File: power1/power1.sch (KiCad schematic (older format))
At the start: 24 parts, among them P1 CONN_01X02, P2 CONN_01X04, U1 LT3633

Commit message: Few more pcb changes
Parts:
- added C13: DNI, Capacitors_Tantalum_SMD:TantalC_SizeC_EIA-6032_HandSoldering, symbol CP1
- added C14: DNI, Capacitors_SMD:C_0805_HandSoldering, symbol C
- C5: footprint Capacitors_SMD:C_0805_HandSoldering -> Capacitors_Tantalum_SMD:TantalC_SizeC_EIA-6032_HandSoldering
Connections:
- net GND: now also C13.2, C14.2
- net at L5.2, P2.4 (P4), U1.18 (Vin2)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: now also C13.1, C14.1
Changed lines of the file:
@@
 F 0 "C5" H 4450 3250 50  0000 L CNN
 F 1 "10uF 25V" H 4450 3050 50  0000 L CNN
-F 2 "Capacitors_SMD:C_0805_HandSoldering" H 4400 3150 60  0001 C CNN
+F 2 "Capacitors_Tantalum_SMD:TantalC_SizeC_EIA-6032_HandSoldering" H 4400 3150 60  0001 C CNN
 F 3 "" H 4400 3150 60  0000 C CNN
 	1    4400 3150
@@
 Text Notes 7300 4300 0    50   ~ 0
 SRP4020TA-1R0M
+$Comp
+L C C14
+U 1 1 54BD0736
+P 9300 3300
+F 0 "C14" H 9300 3400 40  0000 L CNN
+F 1 "DNI" H 9306 3215 40  0000 L CNN
+F 2 "Capacitors_SMD:C_0805_HandSoldering" H 9338 3150 30  0001 C CNN
+F 3 "" H 9300 3300 60  0000 C CNN
+	1    9300 3300
+	1    0    0    -1
+$EndComp
+$Comp
+L GND #PWR016
+U 1 1 54BD07E1
+P 9300 3500
+F 0 "#PWR016" H 9300 3500 30  0001 C CNN
+F 1 "GND" H 9300 3430 30  0001 C CNN
+F 2 "" H 9300 3500 50  0000 C CNN
+F 3 "" H 9300 3500 50  0000 C CNN
+	1    9300 3500
+	1    0    0    -1
+$EndComp
+$Comp
+L CP1 C13
+U 1 1 54BD08E0
+P 8900 3300
+F 0 "C13" H 8950 3400 50  0000 L CNN
+F 1 "DNI" H 8950 3200 50  0000 L CNN
+F 2 "Capacitors_Tantalum_SMD:TantalC_SizeC_EIA-6032_HandSoldering" H 8900 3300 60  0001 C CNN
+F 3 "" H 8900 3300 60  0000 C CNN
+	1    8900 3300
+	1    0    0    -1
+$EndComp
+$Comp
+L GND #PWR017
+U 1 1 54BD0994
+P 8900 3500
+F 0 "#PWR017" H 8900 3500 30  0001 C CNN
+F 1 "GND" H 8900 3430 30  0001 C CNN
+F 2 "" H 8900 3500 50  0000 C CNN
+F 3 "" H 8900 3500 50  0000 C CNN
+	1    8900 3500
+	1    0    0    -1
+$EndComp
+Connection ~ 8900 3100
+Connection ~ 9300 3100
+Connection ~ 8900 3500
+Connection ~ 9300 3500
 $EndSCHEMATC

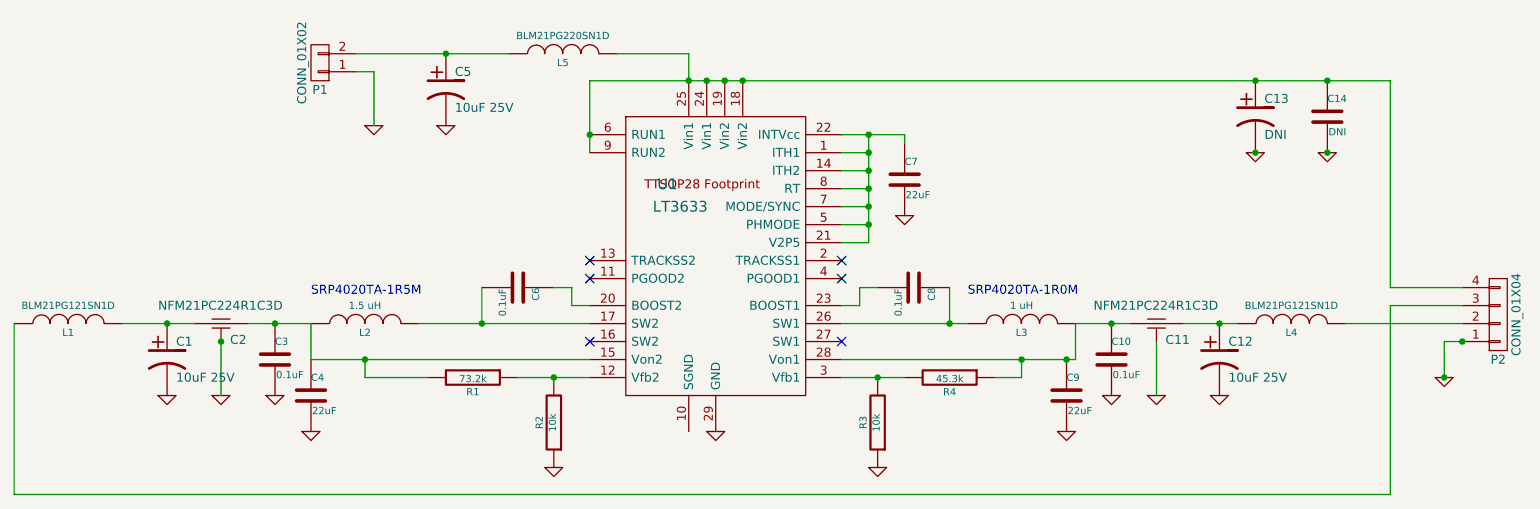
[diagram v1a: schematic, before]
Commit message: Add SGND to circuit
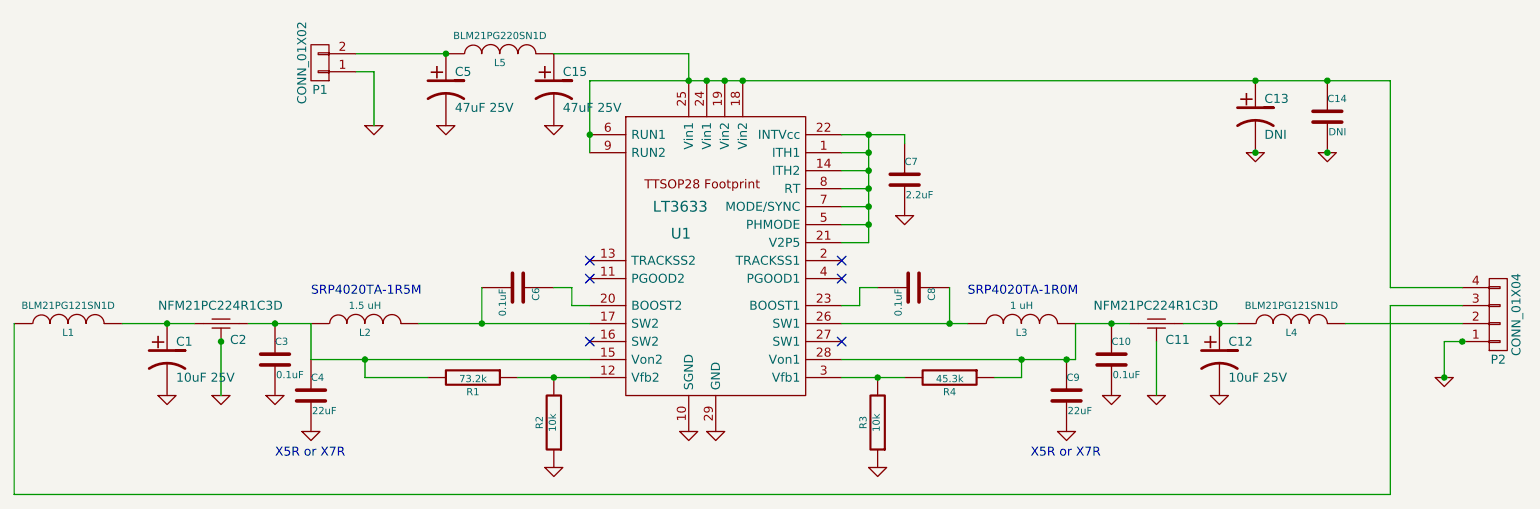
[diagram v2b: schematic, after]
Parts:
- added C15: 47uF 25V, Capacitors_Tantalum_SMD:TantalC_SizeC_EIA-6032_HandSoldering, symbol CP1
- C5: value 10uF 25V -> 47uF 25V
- C7: value 22uF -> 2.2uF
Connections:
- net GND: now also U1.10 (SGND), C15.2
- net at C13.1, C14.1, L5.2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: now also C15.1
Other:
- note added: "X5R or X7R"
- moved on the sheet: L5
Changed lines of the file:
@@
 P 4400 3150
 F 0 "C5" H 4450 3250 50  0000 L CNN
-F 1 "10uF 25V" H 4450 3050 50  0000 L CNN
+F 1 "47uF 25V" H 4450 3050 50  0000 L CNN
 F 2 "Capacitors_Tantalum_SMD:TantalC_SizeC_EIA-6032_HandSoldering" H 4400 3150 60  0001 C CNN
 F 3 "" H 4400 3150 60  0000 C CNN
@@
 U 1 1 54B984F2
 P 5900 3950
-F 0 "U1" H 5575 4225 60  0000 L CNN
+F 0 "U1" H 5650 3950 60  0000 L CNN
 F 1 "LT3633" H 5550 4100 60  0000 L CNN
 F 2 "SMD_Packages:TSSOP-28" H 5900 3550 60  0001 C CNN
@@
 P 6950 3650
 F 0 "C7" H 6950 3750 40  0000 L CNN
-F 1 "22uF" H 6956 3565 40  0000 L CNN
+F 1 "2.2uF" H 6956 3565 40  0000 L CNN
 F 2 "Capacitors_SMD:C_0805_HandSoldering" H 6988 3500 30  0001 C CNN
 F 3 "" H 6950 3650 60  0000 C CNN
@@
 L INDUCTOR L5
 U 1 1 54BA4EF4
-P 5050 2950
-F 0 "L5" V 5000 2950 40  0000 C CNN
-F 1 "BLM21PG220SN1D" V 5150 2950 40  0000 C CNN
-F 2 "SMD_Packages:SMD-0805" H 5050 2950 60  0001 C CNN
-F 3 "" H 5050 2950 60  0000 C CNN
-	1    5050 2950
+P 4700 2950
+F 0 "L5" V 4650 2950 40  0000 C CNN
+F 1 "BLM21PG220SN1D" V 4800 2950 40  0000 C CNN
+F 2 "SMD_Packages:SMD-0805" H 4700 2950 60  0001 C CNN
+F 3 "" H 4700 2950 60  0000 C CNN
+	1    4700 2950
 	0    -1   -1   0
 $EndComp
 Wire Wire Line
-	3900 2950 4750 2950
-Wire Wire Line
-	5350 2950 5750 2950
+	5000 2950 5750 2950
 $Comp
 L GND #PWR014
@@
 Connection ~ 8900 3500
 Connection ~ 9300 3500
+$Comp
+L GND #PWR018
+U 1 1 54BE512A
+P 5750 5050
+F 0 "#PWR018" H 5750 5050 30  0001 C CNN
+F 1 "GND" H 5750 4980 30  0001 C CNN
+F 2 "" H 5750 5050 50  0000 C CNN
+F 3 "" H 5750 5050 50  0000 C CNN
+	1    5750 5050
+	1    0    0    -1
+$EndComp
+$Comp
+L CP1 C15
+U 1 1 54BE5749
+P 5000 3150
+F 0 "C15" H 5050 3250 50  0000 L CNN
+F 1 "47uF 25V" H 5050 3050 50  0000 L CNN
+F 2 "Capacitors_Tantalum_SMD:TantalC_SizeC_EIA-6032_HandSoldering" H 5000 3150 60  0001 C CNN
+F 3 "" H 5000 3150 60  0000 C CNN
+	1    5000 3150
+	1    0    0    -1
+$EndComp
+$Comp
+L GND #PWR?
+U 1 1 54BE578A
+P 5000 3350
+F 0 "#PWR?" H 5000 3350 30  0001 C CNN
+F 1 "GND" H 5000 3280 30  0001 C CNN
+F 2 "" H 5000 3350 50  0000 C CNN
+F 3 "" H 5000 3350 50  0000 C CNN
+	1    5000 3350
+	1    0    0    -1
+$EndComp
+Wire Wire Line
+	3900 2950 4400 2950
+Text Notes 7650 5200 0    50   ~ 0
+X5R or X7R
+Text Notes 3450 5200 0    50   ~ 0
+X5R or X7R
 $EndSCHEMATC
